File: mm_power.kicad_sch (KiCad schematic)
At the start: 1 part, among them J5 Conn_01x02

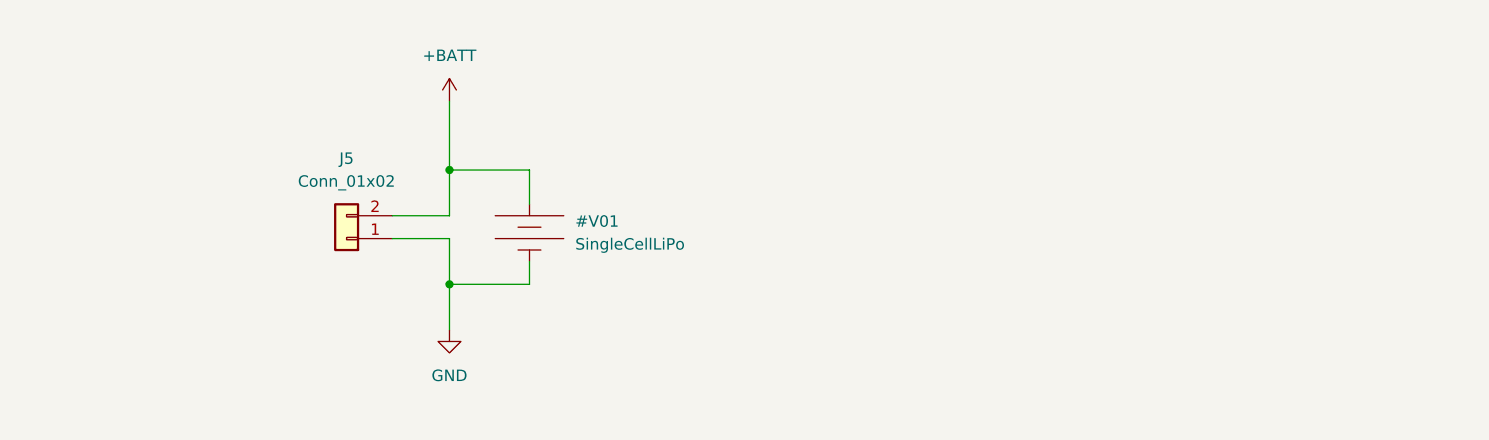
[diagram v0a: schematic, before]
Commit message: ended PCB + added reverse voltage protection
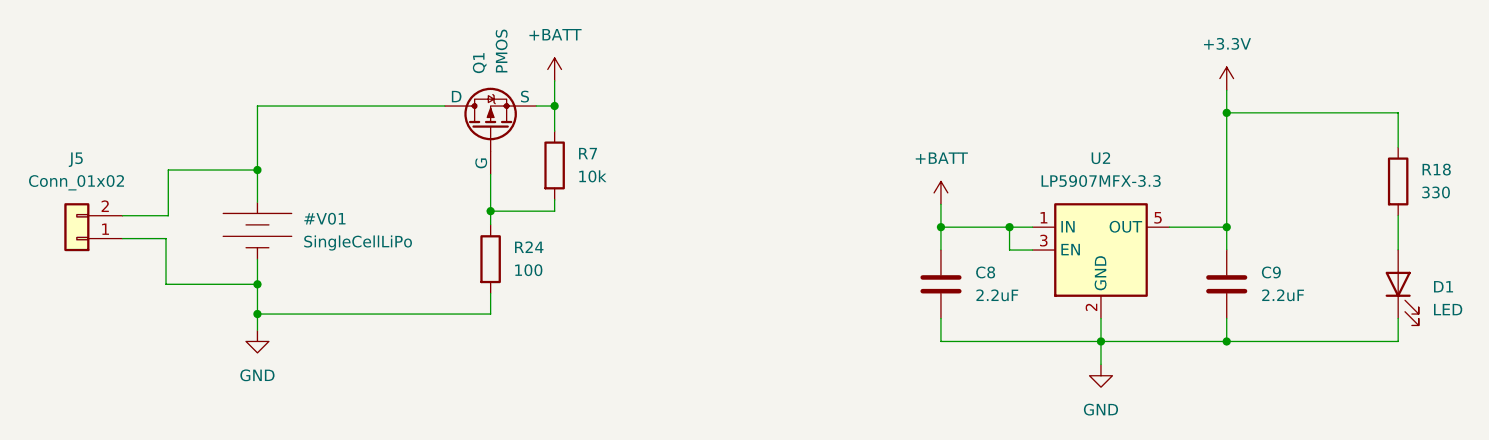
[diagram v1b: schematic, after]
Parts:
- added C8, C9: 2.2uF, Capacitor_SMD:C_0603_1608Metric, symbol Device:C
- added D1: LED, LED_SMD:LED_0603_1608Metric, symbol Device:LED
- added Q1: PMOS, Package_TO_SOT_SMD:SOT-23-3, symbol Simulation_SPICE:PMOS
- added R18: 330, Resistor_SMD:R_0603_1608Metric, symbol Device:R
- added R24: 100, Resistor_SMD:R_0603_1608Metric, symbol Device:R
- added R7: 10k, Resistor_SMD:R_0603_1608Metric, symbol Device:R
- added U2: LP5907MFX-3.3, Package_TO_SOT_SMD:SOT-23-5, symbol Regulator_Linear:LP5907MFX-3.3
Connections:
- net +BATT: now also C8.1, Q1.3 (S), R7.1, U2.1 (IN), U2.3 (EN); no longer J5.2 (Pin_2)
- net GND: now also C8.2, C9.2, D1.1 (K), R24.2, U2.2 (GND)
- new net: Q1.2 (G), R24.1, R7.2
- new net: D1.2 (A), R18.2
- new net: J5.2 (Pin_2), Q1.1 (D)
- new net +3.3V: C9.1, R18.1, U2.5 (OUT)
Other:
- moved on the sheet: J5
